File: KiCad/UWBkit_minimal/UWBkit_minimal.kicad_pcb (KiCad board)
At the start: 2 copper layers, 49 x 39.1 mm, 42 parts, among them J1 Conn_SWD, J2 Conn_BATT, J3 Conn_UART, J7 USB_C_Receptacle_USB2.0_14P, Q1 BSS341, Q2 BSS138, Q3 BSS138, SW1 SW_Push, U2 MAX40203AUK+T, U3 DWM3001C, U4 XC9285B33CMR-G, U6 IP4234CZ6

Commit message: Progress on minimal design
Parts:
- moved SW1 28.9 mm to (139.4, 64.2)
- moved J3 15.2 mm to (172.6, 77.2), turned to 0 degrees
- moved Q3 10.6 mm to (164.5, 68.7), turned to 90 degrees
- moved R9 9.70 mm to (167.9, 65.8), turned to 0 degrees
- moved R10 9.60 mm to (164.7, 65.8), turned to 0 degrees
- moved D5 8.10 mm to (166.3, 72.5), turned to 0 degrees
- moved R5 7.90 mm to (164.8, 75.7), turned to 90 degrees
- moved D4 6.97 mm to (163.9, 85.9), turned to -90 degrees
- moved Q2 6.80 mm to (168.1, 68.7)
- moved R4 6.39 mm to (166.3, 75.7), turned to 90 degrees
- moved R1 5.74 mm to (163.9, 82.3), turned to 90 degrees
- moved R3 5.49 mm to (167.8, 75.7), turned to 90 degrees
- moved D3 5.14 mm to (165.5, 85.9), turned to -90 degrees
- moved D1 4.36 mm to (168.7, 85.9), turned to -90 degrees
- moved D2 4.08 mm to (167.1, 85.9), turned to -90 degrees
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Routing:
- net +3V3: track 20.9 -> 95.8 mm, vias 0 -> 3
- net /SWDIO: track 0.00 -> 19.2 mm
- net /SWCLK: track 0.00 -> 17.8 mm
- net /RXD: track 0.00 -> 13.9 mm
- net /TXD: track 0.00 -> 11.7 mm, vias 0 -> 2
- net /RESET: track 32.8 -> 44.0 mm
- net SOC_VBUS: track 37.5 -> 46.8 mm, vias 5 -> 4
- net /RX_LED: track 0.00 -> 6.93 mm
- net /SOC_D-: track 4.92 -> 11.7 mm, vias 2 -> 0
- net Net-(U3-P0.22): track 25.1 -> 31.7 mm
- net Net-(U3-P0.14): track 25.8 -> 30.9 mm
- net /SOC_D+: track 7.41 -> 12.4 mm, vias 2 -> 0
- net Net-(D5-A1): track 8.48 -> 4.26 mm
- net Net-(U3-P0.05): track 24.4 -> 28.1 mm
- net /TX_LED: track 0.00 -> 3.46 mm
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
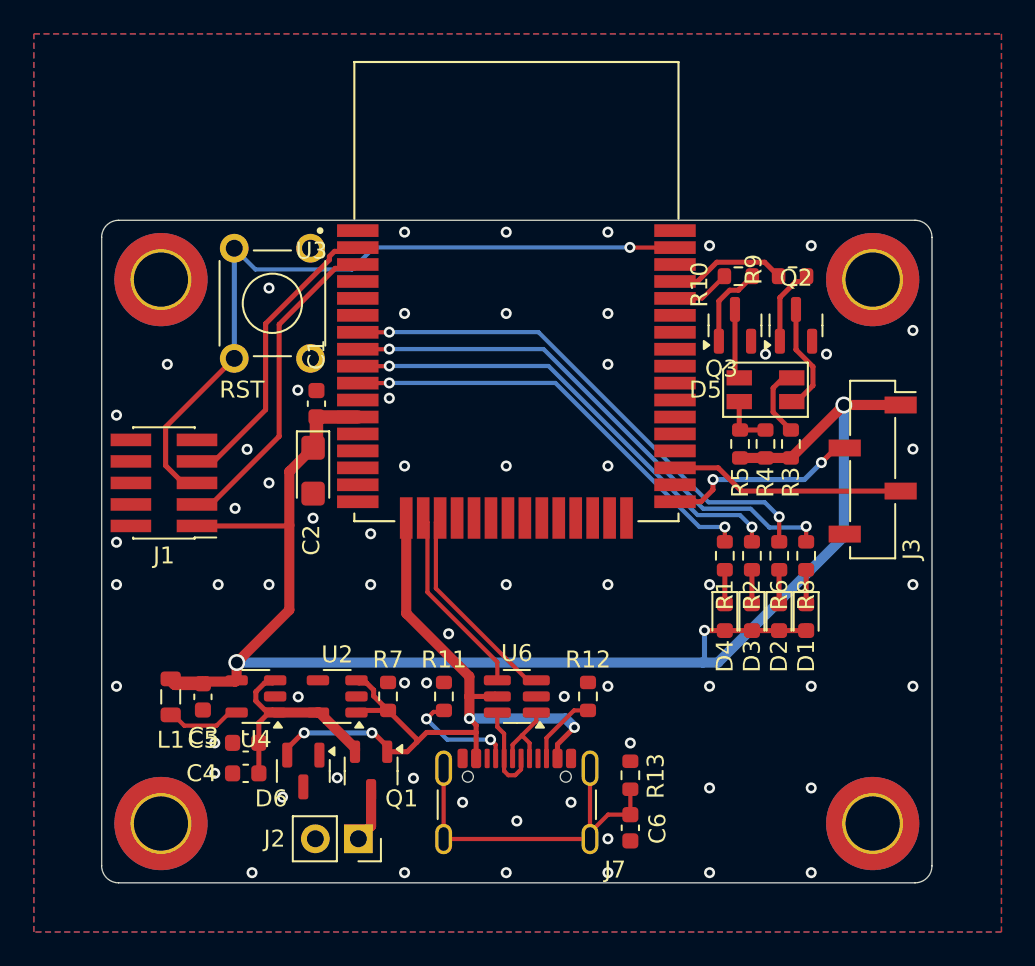
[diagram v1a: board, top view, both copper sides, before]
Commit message: Added power led, test points, modified layout
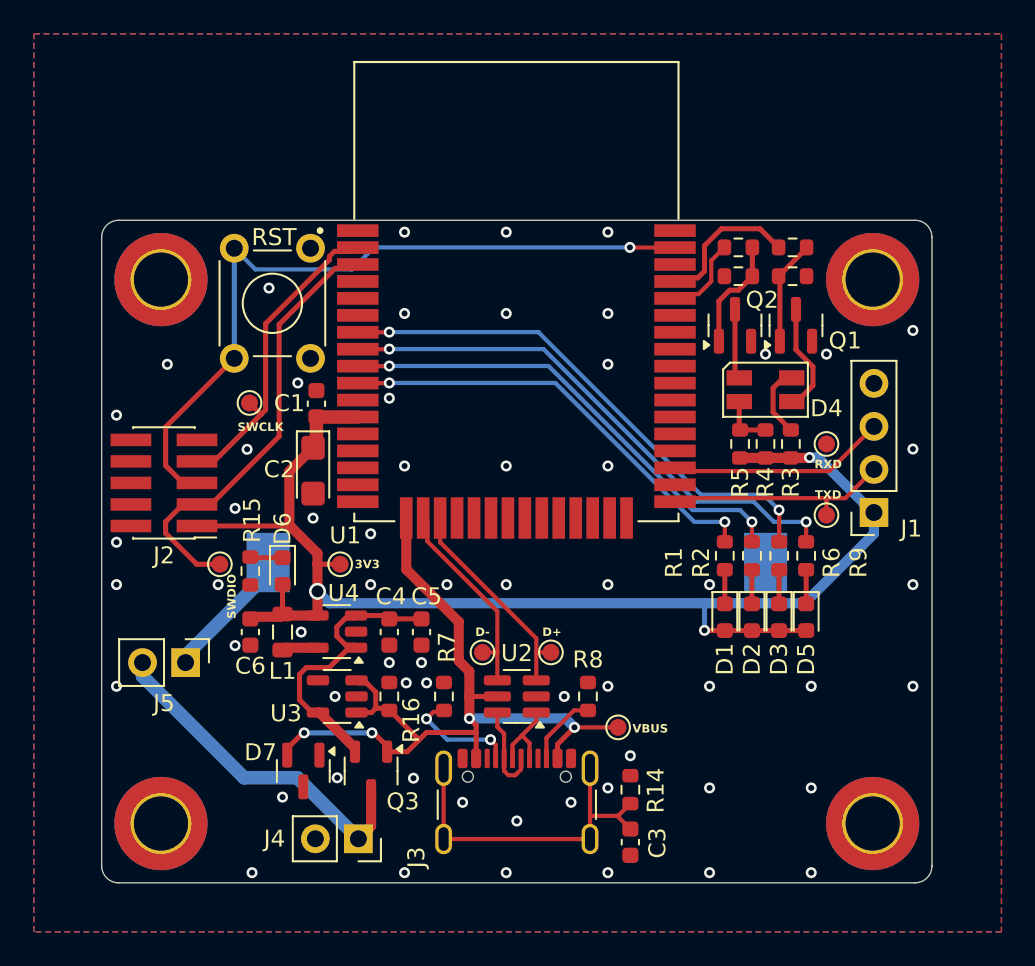
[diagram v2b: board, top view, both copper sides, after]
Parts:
- added BT1: CR2032, Battery:BatteryHolder_Keystone_1058_1x2032, B.Cu at (151.6, 82.7)
- added D6: R, LED_SMD:LED_0603_1608Metric, F.Cu at (137.8, 83.2)
- added J5: Jumper_Cell_NO, Connector_PinHeader_2.54mm:PinHeader_1x02_P2.54mm_Vertical, F.Cu at (132.1, 88.6)
- added R12: 100k, Resistor_SMD:R_0603_1608Metric, F.Cu at (167.9, 65.8)
- added R13: 100k, Resistor_SMD:R_0603_1608Metric, F.Cu at (164.7, 65.8)
- added R15: 1k, Resistor_SMD:R_0603_1608Metric, F.Cu at (135.9, 83.2)
- added TP1: TestPoint_Small, TestPoint:TestPoint_Pad_D1.0mm, F.Cu at (149.6, 88.0)
- added TP2: TestPoint_Small, TestPoint:TestPoint_Pad_D1.0mm, F.Cu at (153.6, 88.0)
- added TP3: TestPoint_Small, TestPoint:TestPoint_Pad_D1.0mm, F.Cu at (157.6, 92.4)
- added TP4: TestPoint_Small, TestPoint:TestPoint_Pad_D1.0mm, F.Cu at (141.2, 82.8)
- added TP5: TestPoint_Small, TestPoint:TestPoint_Pad_D1.0mm, F.Cu at (169.9, 79.9)
- added TP6: TestPoint_Small, TestPoint:TestPoint_Pad_D1.0mm, F.Cu at (169.9, 75.7)
- added TP7: TestPoint_Small, TestPoint:TestPoint_Pad_D1.0mm, F.Cu at (134.1, 82.8)
- added TP8: TestPoint_Small, TestPoint:TestPoint_Pad_D1.0mm, F.Cu at (135.9, 73.3)
- J1: renamed from J3; footprint Connector_PinSocket_2.54mm:PinSocket_1x04_P2.54mm_Vertical_SMD_Pin1Right -> Connector_PinSocket_2.54mm:PinSocket_1x04_P2.54mm_Vertical
- moved C5 13.3 mm to (146.0, 86.8), turned to -90 degrees
- moved C4 10.7 mm to (144.1, 86.8), turned to -90 degrees
- moved L1 7.63 mm to (137.8, 86.8)
- moved U4 6.12 mm to (141.0, 86.8)
- moved C6 4.74 mm to (135.9, 86.8)
- moved J1 2.54 mm to (172.7, 79.7), turned to 180 degrees
- moved R10 1.70 mm to (167.9, 64.1)
- moved R11 1.70 mm to (164.7, 64.1)
- moved C3 0.85 mm to (158.3, 99.2)
- moved R14 0.85 mm to (158.3, 96.1)
- moved R16 0.07 mm to (144.1, 90.6)
- renumbered C6 to C3, C3 to C4, C4 to C5, C5 to C6, D4 to D1, D3 to D2, D2 to D3, D5 to D4, D1 to D5, D6 to D7, J1 to J2, J7 to J3, J2 to J4, Q2 to Q1, Q3 to Q2, Q1 to Q3, R9 to R10, R10 to R11, R13 to R14, R7 to R16, R11 to R7, R12 to R8, R8 to R9, U3 to U1, U6 to U2, U2 to U3
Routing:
- net V_BATT: track 3.17 -> 21.1 mm
- net +3V3: track 95.8 -> 81.2 mm
- net Net-(BT1-+): track 0.00 -> 7.52 mm
- net /SWDIO: track 19.2 -> 26.1 mm
- net Net-(Q3-S): track 14.5 -> 18.9 mm
- net SOC_VBUS: track 46.8 -> 49.2 mm
- net Net-(U4-Lx): track 4.47 -> 2.12 mm
- net Net-(D6-K): track 0.00 -> 1.92 mm
- net /TXD: track 11.7 -> 13.5 mm, vias 2 -> 0
- net /RX_LED: track 6.93 -> 8.74 mm
- net Net-(Q2-G): track 4.96 -> 6.66 mm
- net Net-(Q1-G): track 4.72 -> 6.25 mm
- net /TX_LED: track 3.46 -> 4.88 mm
- net /RXD: track 13.9 -> 12.9 mm
- net /SWCLK: track 17.8 -> 18.8 mm
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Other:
- board text added: "3V3"
- board text added: "CR2032"
- board text added: "D+"
- board text added: "D-"
- board text added: "RXD"
- board text added: "SWCLK"
- board text added: "SWDIO"
- board text added: "TXD"
- board text added: "VBUS"

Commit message: Minor additions
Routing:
- net /RXD: track 12.9 -> 14.2 mm
- net GND: vias 61 -> 66
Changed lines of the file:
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@@
 	)
 	(via
-		(at 169.9 70.4)
+		(at 170 71)
 		(size 0.65)
 		(drill 0.35)
@@
 	)
 	(via
-		(at 154.825 96.85)
+		(at 155 97)
 		(size 0.65)
 		(drill 0.35)
@@
 	)
 	(via
-		(at 138.9 86.8)
-		(size 0.65)
-		(drill 0.35)
-		(layers "F.Cu" "B.Cu")
-		(free yes)
-		(net 3)
-	)
-	(via
-		(at 154.425 90.6)
+		(at 139 86.8)
+		(size 0.65)
+		(drill 0.35)
+		(layers "F.Cu" "B.Cu")
+		(free yes)
+		(net 3)
+	)
+	(via
+		(at 154.11781 90.617116)
 		(size 0.65)
 		(drill 0.35)
@@
 	)
 	(via
+		(at 163 74)
+		(size 0.65)
+		(drill 0.35)
+		(layers "F.Cu" "B.Cu")
+		(free yes)
+		(net 3)
+	)
+	(via
 		(at 175 69)
 		(size 0.65)
@@
 	)
 	(via
+		(at 166 68)
+		(size 0.65)
+		(drill 0.35)
+		(layers "F.Cu" "B.Cu")
+		(free yes)
+		(net 3)
+	)
+	(via
 		(at 151.625 97.95)
 		(size 0.65)
@@
 	)
 	(via
+		(at 167.886222 63.051259)
+		(size 0.65)
+		(drill 0.35)
+		(layers "F.Cu" "B.Cu")
+		(free yes)
+		(net 3)
+	)
+	(via
 		(at 169 90)
 		(size 0.65)
@@
 	)
 	(via
+		(at 163 78)
+		(size 0.65)
+		(drill 0.35)
+		(layers "F.Cu" "B.Cu")
+		(free yes)
+		(net 3)
+	)
+	(via
 		(at 157 96)
 		(size 0.65)
@@
 	)
 	(via
+		(at 135.7 68)
+		(size 0.65)
+		(drill 0.35)
+		(layers "F.Cu" "B.Cu")
+		(free yes)
+		(net 3)
+	)
+	(via
 		(at 163 84)
 		(size 0.65)
@@
 	)
 	(via
-		(at 137 66.5)
-		(size 0.65)
-		(drill 0.35)
-		(layers "F.Cu" "B.Cu")
-		(free yes)
-		(net 3)
-	)
-	(via
 		(at 145.525 95.425)
 		(size 0.65)
@@
 	)
 	(via
-		(at 137.8 96.54)
+		(at 136 97)
 		(size 0.65)
 		(drill 0.35)
@@
 	)
 	(via
-		(at 148.425 96.85)
+		(at 168.888908 78.150351)
+		(size 0.65)
+		(drill 0.35)
+		(layers "F.Cu" "B.Cu")
+		(free yes)
+		(net 3)
+	)
+	(via
+		(at 148 97)
 		(size 0.65)
 		(drill 0.35)
@@
 	)
 	(via
-		(at 166.3 70.4)
+		(at 166 71)
 		(size 0.65)
 		(drill 0.35)
@@
 	)
 	(segment
+		(start 170.7825 76.5825)
+		(end 172.7 74.665)
+		(width 0.25)
+		(layer "F.Cu")
+		(net 13)
+	)
+	(segment
+		(start 169.9 75.7)
+		(end 170.7825 76.5825)
+		(width 0.25)
+		(layer "F.Cu")
+		(net 13)
+	)
+	(segment
 		(start 170.065 77.3)
-		(end 172.7 74.665)
-		(width 0.25)
-		(layer "F.Cu")
+		(end 170.7825 76.5825)
+		(width 0.25)
+		(layer "F.Cu")

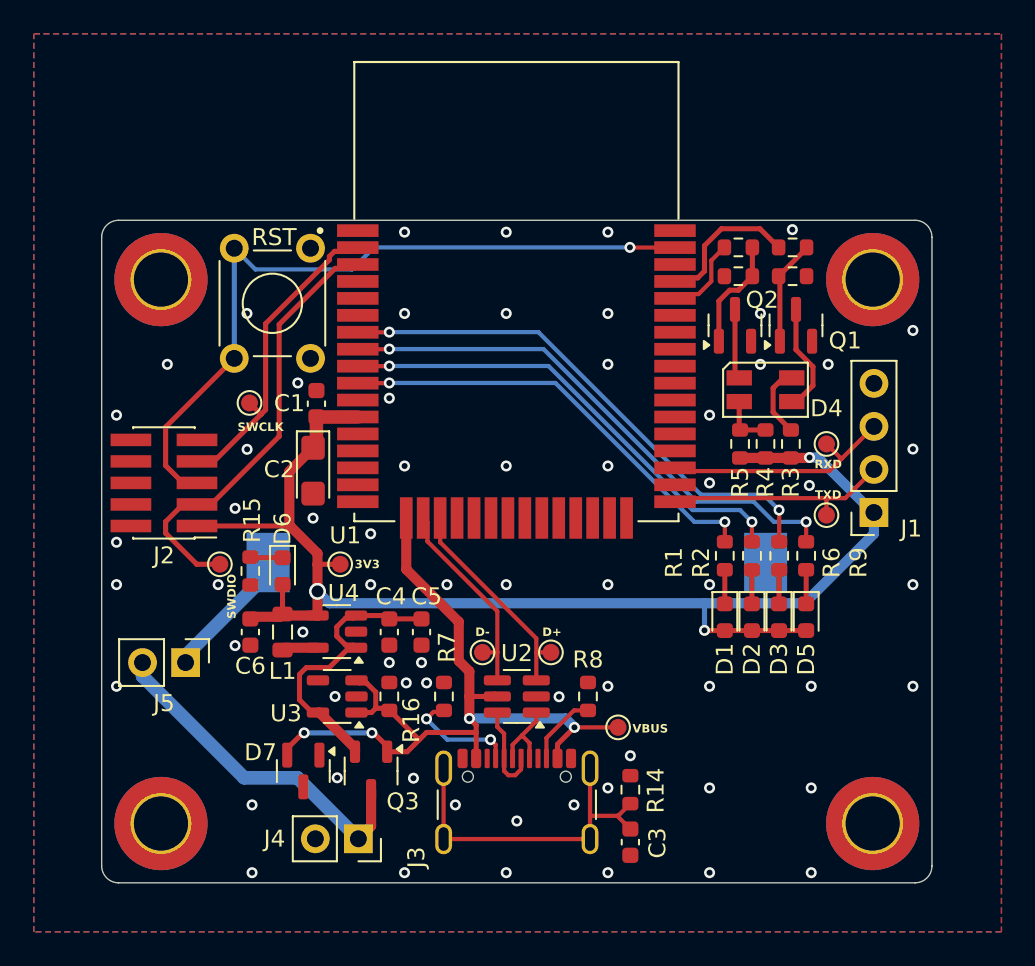
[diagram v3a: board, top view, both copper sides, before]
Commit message: Minor changes, added a footprint with QR code
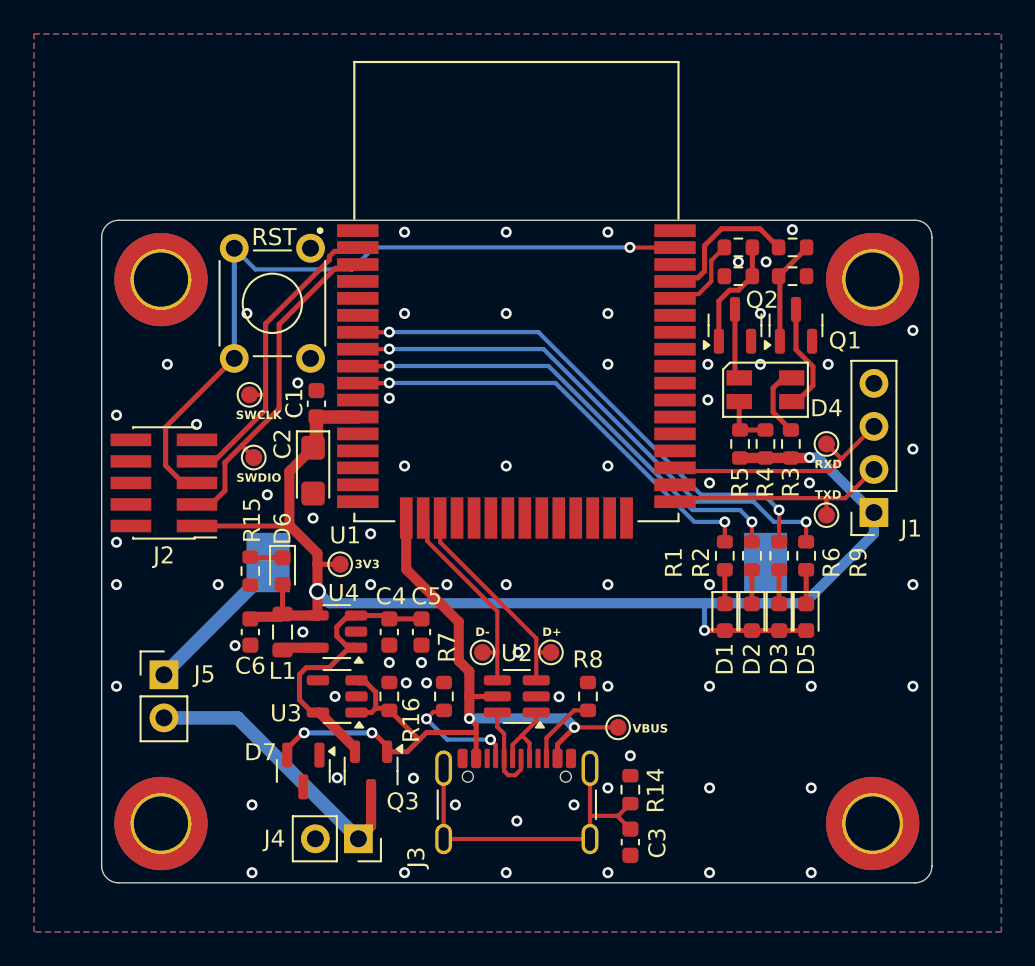
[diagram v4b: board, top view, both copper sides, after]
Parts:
- added QR*****: , UWBkit:Git_QR, B.Cu at (164.0, 95.9)
- R1: value 1k -> 200R
- R15, R6, R9: value 1k -> 300R
- R2: value 1k -> 30R
- moved TP1 6.61 mm to (136.1, 76.5)
- moved J5 1.47 mm to (130.8, 89.3), turned to 0 degrees
- moved TP4 0.48 mm to (135.9, 72.8)
- renumbered TP7 to TP1, TP5 to TP2, TP6 to TP3, TP8 to TP4, TP3 to TP5, TP1 to TP6, TP2 to TP7, TP4 to TP8
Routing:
- net /SWDIO: track 26.1 -> 21.0 mm
- net V_BATT: track 21.1 -> 17.6 mm
- net Net-(BT1-+): track 7.52 -> 9.80 mm
- net GND: vias 66 -> 70
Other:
- board text added: "PCB3D_BR_uwb"
- board text added: "PCB3D_TL_uwb"

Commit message: Generated BOM
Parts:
- D4: value LSG T676 -> LSG T676-P7R-1-0+N7P9-24
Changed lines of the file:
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@@
 		(sheetname "/")
 		(sheetfile "UWBkit_minimal.kicad_sch")
-		(attr exclude_from_pos_files)
+		(attr exclude_from_pos_files exclude_from_bom)
 		(fp_circle
 			(center 0 0)
@@
 			)
 		)
+		(property "Current" "5 mA"
+			(at 0 0 270)
+			(unlocked yes)
+			(layer "F.Fab")
+			(hide yes)
+			(effects
+				(font
+					(size 1 1)
+					(thickness 0.15)
+				)
+			)
+		)
 		(property ki_fp_filters "LED* LED_SMD:* LED_THT:*")
 		(sheetname "/")
@@
 		(sheetname "/")
 		(sheetfile "UWBkit_minimal.kicad_sch")
-		(attr exclude_from_pos_files)
+		(attr exclude_from_pos_files exclude_from_bom)
 		(fp_circle
 			(center 0 0)
@@
 		(sheetname "/")
 		(sheetfile "UWBkit_minimal.kicad_sch")
-		(attr exclude_from_pos_files)
+		(attr exclude_from_pos_files exclude_from_bom)
 		(fp_circle
 			(center 0 0)
@@
 		(sheetname "/")
 		(sheetfile "UWBkit_minimal.kicad_sch")
-		(attr exclude_from_pos_files)
+		(attr exclude_from_pos_files exclude_from_bom)
 		(fp_circle
 			(center 0 0)
@@
 			)
 		)
+		(property "Current" "2 mA"
+			(at 0 0 270)
+			(unlocked yes)
+			(layer "F.Fab")
+			(hide yes)
+			(effects
+				(font
+					(size 1 1)
+					(thickness 0.15)
+				)
+			)
+		)
 		(property ki_fp_filters "LED* LED_SMD:* LED_THT:*")
 		(sheetname "/")
@@
 		(sheetname "/")
 		(sheetfile "UWBkit_minimal.kicad_sch")
-		(attr exclude_from_pos_files)
+		(attr exclude_from_pos_files exclude_from_bom)
 		(fp_circle
 			(center 0 0)
@@
 			)
 		)
+		(property "Current" "7 mA"
+			(at 0 0 270)
+			(unlocked yes)
+			(layer "F.Fab")
+			(hide yes)
+			(effects
+				(font
+					(size 1 1)
+					(thickness 0.15)
+				)
+			)
+		)
 		(property ki_fp_filters "LED* LED_SMD:* LED_THT:*")
 		(sheetname "/")
@@
 			)
 		)
+		(property "Current" "5 mA"
+			(at 0 0 270)
+			(unlocked yes)
+			(layer "F.Fab")
+			(hide yes)
+			(effects
+				(font
+					(size 1 1)
+					(thickness 0.15)
+				)
+			)
+		)
 		(property ki_fp_filters "LED* LED_SMD:* LED_THT:*")
 		(sheetname "/")
@@
 		(sheetname "/")
 		(sheetfile "UWBkit_minimal.kicad_sch")
-		(attr exclude_from_pos_files)
+		(attr exclude_from_pos_files exclude_from_bom)
 		(fp_circle
 			(center 0 0)
@@
 			)
 		)
+		(property "Current" "5 mA"
+			(at 0 0 270)
+			(unlocked yes)
+			(layer "F.Fab")
+			(hide yes)
+			(effects
+				(font
+					(size 1 1)
+					(thickness 0.15)
+				)
+			)
+		)
 		(property ki_fp_filters "LED* LED_SMD:* LED_THT:*")
 		(sheetname "/")
@@
 		(sheetname "/")
 		(sheetfile "UWBkit_minimal.kicad_sch")
-		(attr exclude_from_pos_files)
+		(attr exclude_from_pos_files exclude_from_bom)
 		(fp_circle
 			(center 0 0)
@@
 			)
 		)
-		(property "Value" "LSG T676"
+		(property "Value" "LSG T676-P7R-1-0+N7P9-24"
 			(at 0 2.5 0)
 			(layer "F.Fab")
@@
 		(sheetname "/")
 		(sheetfile "UWBkit_minimal.kicad_sch")
-		(attr exclude_from_pos_files)
+		(attr exclude_from_pos_files exclude_from_bom)
 		(fp_circle
 			(center 0 0)
@@
 			)
 		)
+		(attr board_only exclude_from_bom)
 		(fp_rect
 			(start 4.05 4.35)

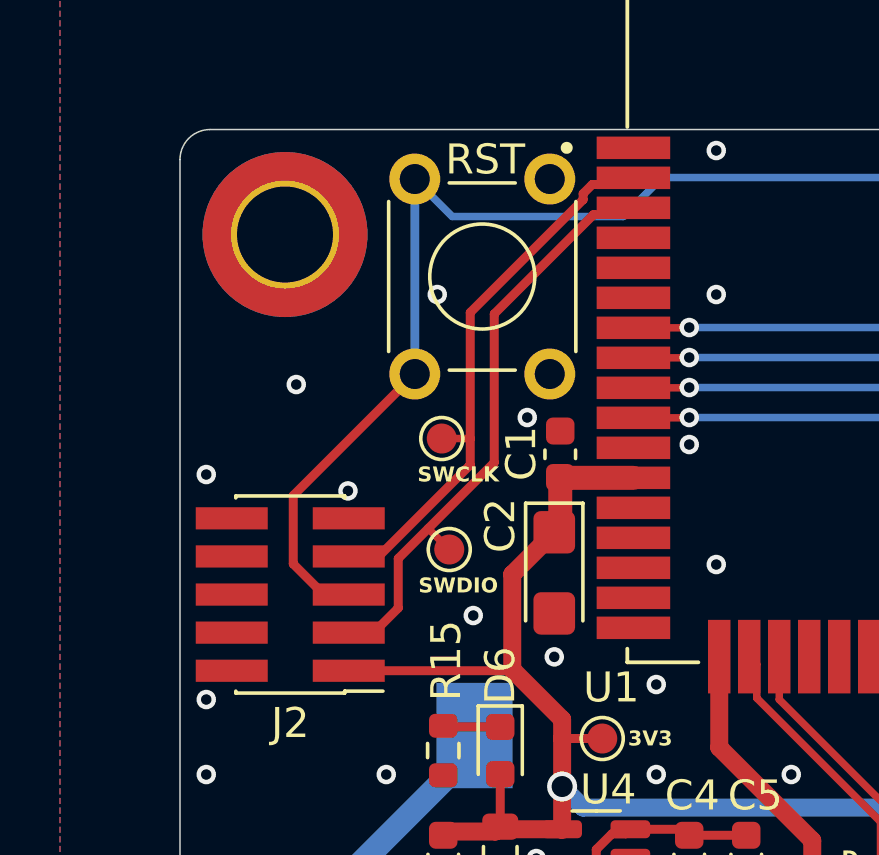
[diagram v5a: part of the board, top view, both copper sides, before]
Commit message: Updated pinout for SWD connector
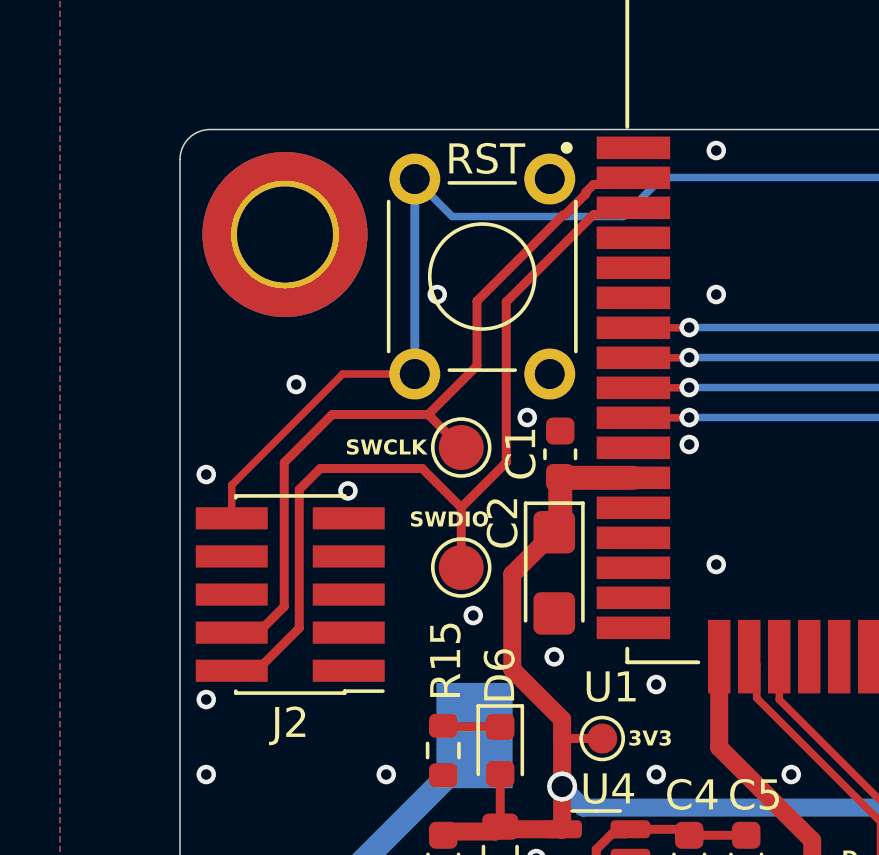
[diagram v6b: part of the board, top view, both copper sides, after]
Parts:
- Q3: value BSS341 -> BSS84
- TP1, TP4: footprint TestPoint:TestPoint_Pad_D1.0mm -> TestPoint:TestPoint_Pad_D1.5mm
- moved TP1 0.72 mm to (136.5, 77.1)
- moved TP4 0.72 mm to (136.5, 73.1)
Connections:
- J2 pad 10: GND -> /RESET
- J2 pad 2: GND -> /SWDIO
- J2 pad 3: /SWDIO -> GND
- J2 pad 4: GND -> /SWCLK
- J2 pad 5: /RESET -> GND
- J2 pad 6: GND -> unconnected-(J2-Pin_6-Pad6)
- J2 pad 7: /SWCLK -> unconnected-(J2-Pin_7-Pad7)
- J2 pad 8: GND -> unconnected-(J2-Pin_8-Pad8)
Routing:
- net /SWDIO: track 21.0 -> 28.7 mm
- net /SWCLK: track 18.8 -> 25.3 mm
- net +3V3: track 81.1 -> 75.7 mm
- net GND: track 0.00 -> 2.49 mm
- net /RESET: track 44.0 -> 42.5 mm
- net unconnected-(J2-Pin_7-Pad7): track 0.00 -> 1.00 mm
